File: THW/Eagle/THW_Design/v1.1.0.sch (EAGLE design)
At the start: 34 parts, among them U1 ADA4091-2ARZ-RL

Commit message: new version
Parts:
- removed JP1: (no value), pinhead:PINHD-2X10
- removed PAD1, PAD2, PAD4: (no value), wirepad:SMD5
- removed WP1: WIREPOINT_1A, WIREPOINT:WIREPOINT_1A
- added JP3: (no value), pinhead:PINHD-2X12
- added LONG_HW-: WIREPOINT_1A, WIREPOINT:WIREPOINT_1A
- added PAD5, PAD6, PAD7: (no value), wirepad:SMD5
- added PT$5, PT$6: PTS1206A, PTS1206:PTS1206A
- added TP1, TP13, TP14, TP15, TP16, TP17, TP18, TP19, TP2, TP20, TP21, TP22, TP23, TP24, TP25, TP26, TP27, TP28, TP3, TP4: TPTP10SQ, testpad:TPTP10SQ
- TP10, TP11, TP12, TP5, TP6, TP7, TP8, TP9: value TPSQTP09SQ -> TPTP10SQ; device testpad:TPSQTP09SQ -> testpad:TPTP10SQ
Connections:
- removed net T_S1+: JP1.1, PT$1.P$1, TP5.TP
- removed net T_S1-: JP1.2, PT$1.P$2, TP6.TP
- removed net T_S2+: JP1.3, PT$2.P$1, TP7.TP
- removed net T_S2-: JP1.4, PT$2.P$2, TP8.TP
- removed net T_S3+: JP1.5, PT$3.P$1, TP9.TP
- removed net T_S3-: JP1.6, PT$3.P$2, TP10.TP
- removed net T_S4+: JP1.7, PT$4.P$1, TP11.TP
- removed net T_S4-: JP1.8, PT$4.P$2, TP12.TP
- new net LONG_HW_SENS+: LONG_HW+.P$2, TP27.TP
- new net LONG_HW_SENS-: LONG_HW-.P$1, TP28.TP
- new net PT1_+: JP3.1, PT$2.+, TP1.TP
- new net PT1_-: JP3.2, PT$2.-, TP3.TP
- new net PT1_S+: JP3.3, PT$2.S+, TP2.TP
- new net PT1_S-: JP3.4, PT$2.S-, TP4.TP
- new net PT2_+: JP3.5, PT$3.+, TP5.TP
- new net PT2_-: JP3.6, PT$3.-, TP7.TP
- new net PT2_S+: JP3.7, PT$3.S+, TP6.TP
- new net PT2_S-: JP3.8, PT$3.S-, TP8.TP
- new net PT3_+: JP3.9, PT$1.+, TP9.TP
- new net PT3_-: JP3.10, PT$1.-, TP11.TP
- new net PT3_S+: JP3.11, PT$1.S+, TP10.TP
- new net PT3_S-: JP3.12, PT$1.S-, TP12.TP
- new net PT4_+: JP3.13, PT$4.+, TP13.TP
- new net PT4_-: JP3.14, PT$4.-, TP15.TP
- new net PT4_S+: JP3.15, PT$4.S+, TP14.TP
- new net PT4_S-: JP3.16, PT$4.S-, TP16.TP
- new net PT5_+: JP3.17, PT$5.+, TP17.TP
- new net PT5_-: JP3.18, PT$5.-, TP19.TP
- new net PT5_S+: JP3.19, PT$5.S+, TP18.TP
- new net PT5_S-: JP3.20, PT$5.S-, TP20.TP
- new net PT6_+: JP3.21, PT$6.+, TP21.TP
- new net PT6_-: JP3.22, PT$6.-, TP23.TP
- new net PT6_S+: JP3.23, PT$6.S+, TP22.TP
- new net PT6_S-: JP3.24, PT$6.S-, TP24.TP
- new net SHORT_HW_SENS+: SHORT_HW+.P$2, TP26.TP
- new net SHORT_HW_SENS-: SHORT_HW-.P$1, TP25.TP
- net LONG_HW+: now also PAD7.P; no longer PAD4.P, SV1.1
- net LONG_HW-: now also LONG_HW-.P$2; no longer SV1.2, WP1.P$1
- net SHORT_HW+: now also PAD5.P; no longer PAD1.P, SV1.35
- net SHORT_HW-: now also PAD6.P, SHORT_HW-.P$2; no longer PAD2.P, SHORT_HW-.P$1, SV1.36
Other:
- note removed: "Nanofluids: THW"
- moved on the sheet: C1, PAD3, R1, R2, R3, U1

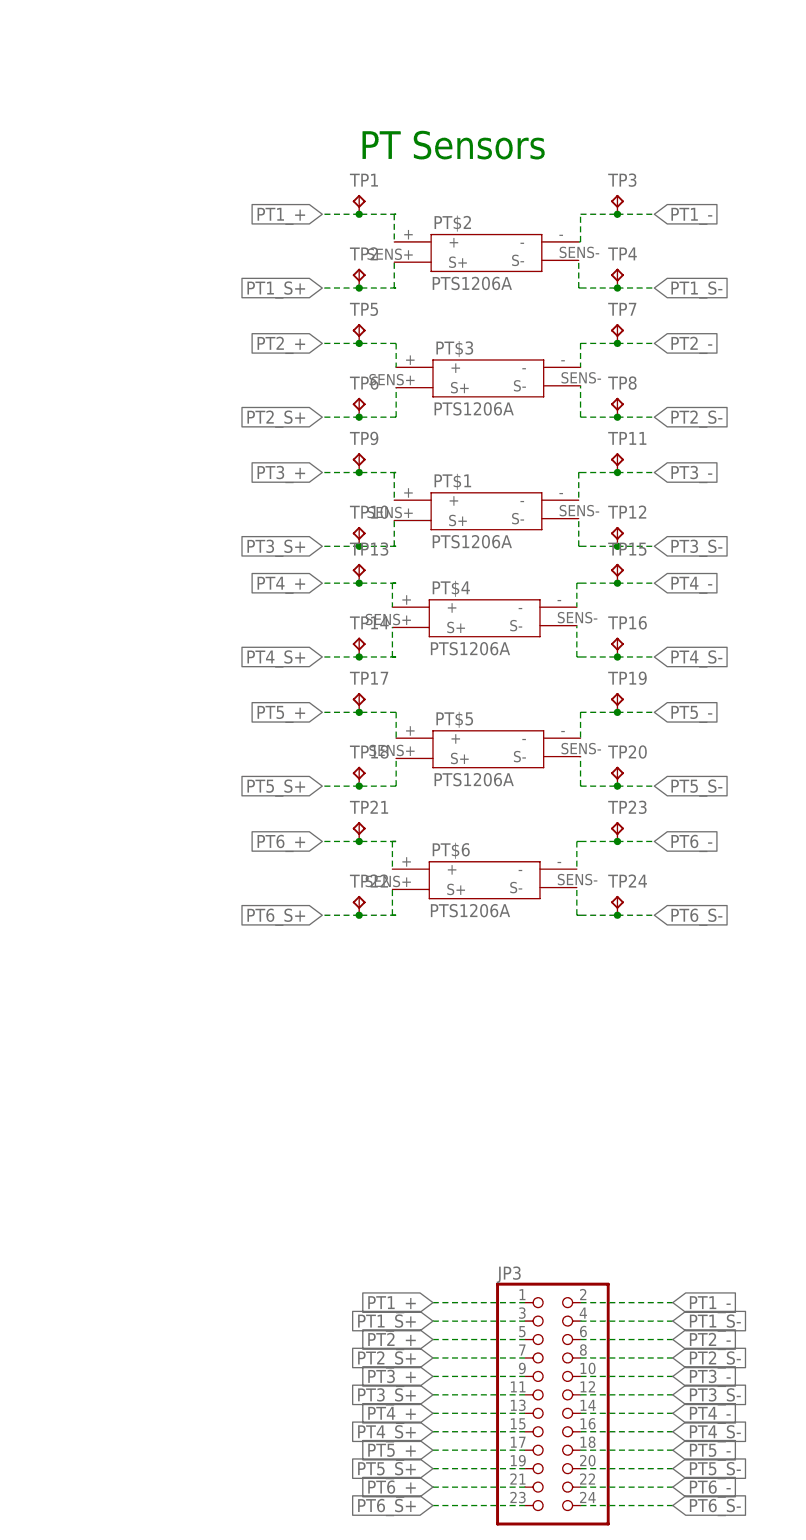
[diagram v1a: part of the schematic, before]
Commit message: adding one current source to PT sensors
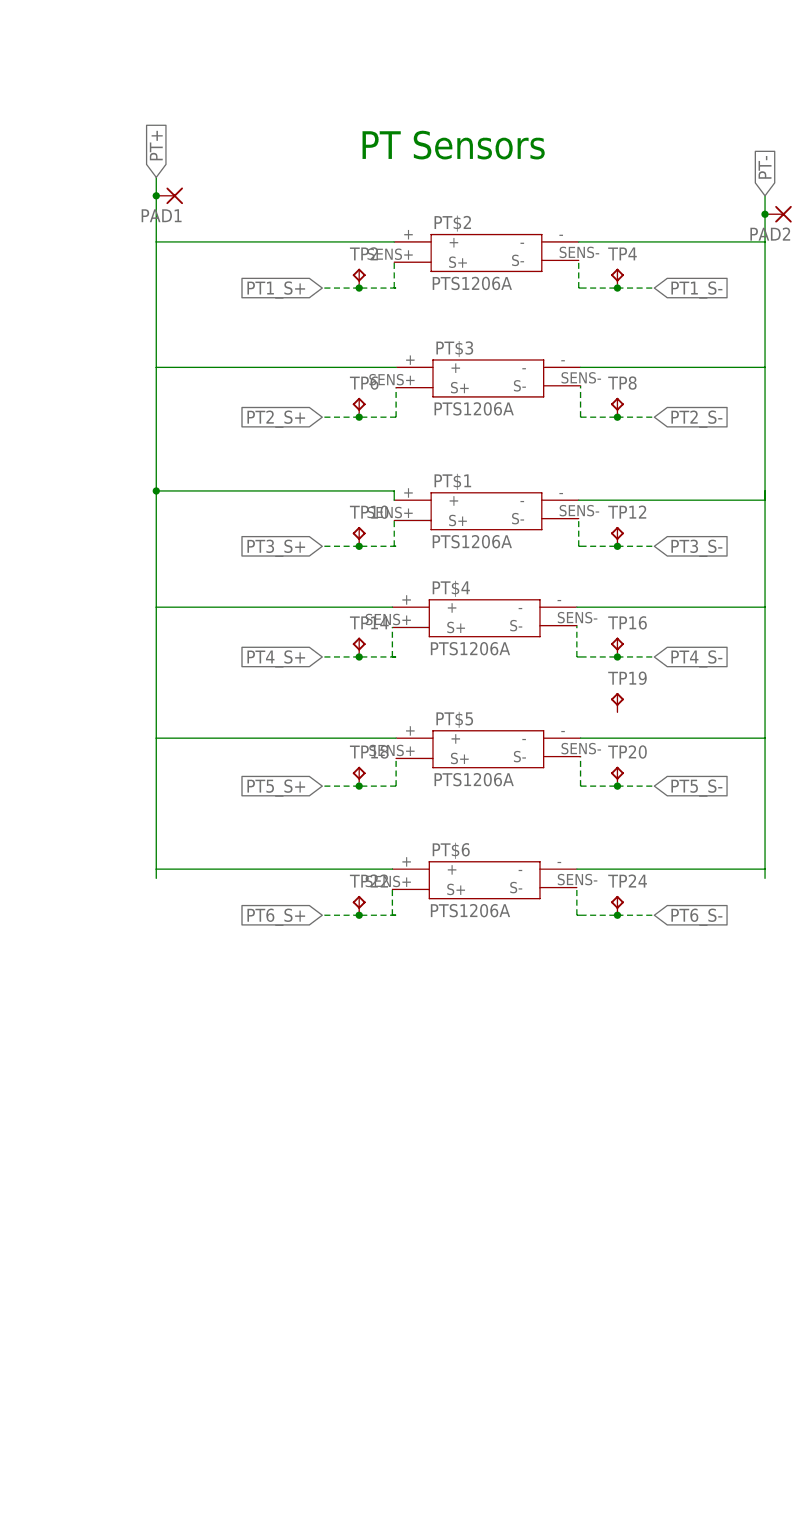
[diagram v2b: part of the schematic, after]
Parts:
- removed JP3: (no value), pinhead:PINHD-2X12
- removed TP1, TP11, TP13, TP15, TP17, TP21, TP23, TP3, TP5, TP7, TP9: TPTP10SQ, testpad:TPTP10SQ
- added PAD1, PAD2: (no value), wirepad:SMD5
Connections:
- removed net PT1_+: JP3.1, PT$2.+, TP1.TP
- removed net PT1_-: JP3.2, PT$2.-, TP3.TP
- removed net PT2_+: JP3.5, PT$3.+, TP5.TP
- removed net PT2_-: JP3.6, PT$3.-, TP7.TP
- removed net PT3_+: JP3.9, PT$1.+, TP9.TP
- removed net PT3_-: JP3.10, PT$1.-, TP11.TP
- removed net PT4_+: JP3.13, PT$4.+, TP13.TP
- removed net PT4_-: JP3.14, PT$4.-, TP15.TP
- removed net PT5_+: JP3.17, PT$5.+, TP17.TP
- removed net PT5_-: JP3.18, PT$5.-, TP19.TP
- removed net PT6_+: JP3.21, PT$6.+, TP21.TP
- removed net PT6_-: JP3.22, PT$6.-, TP23.TP
- new net B$2: PT$1.-
- new net PT+: PAD1.P, PT$1.+, PT$2.+, PT$3.+, PT$4.+, PT$5.+, PT$6.+
- new net PT-: PAD2.P, PT$2.-, PT$3.-, PT$4.-, PT$5.-, PT$6.-
- net PT1_S+: no longer JP3.3
- net PT1_S-: no longer JP3.4
- net PT2_S+: no longer JP3.7
- net PT2_S-: no longer JP3.8
- net PT3_S+: no longer JP3.11
- net PT3_S-: no longer JP3.12
- net PT4_S+: no longer JP3.15
- net PT4_S-: no longer JP3.16
- net PT5_S+: no longer JP3.19
- net PT5_S-: no longer JP3.20
- net PT6_S+: no longer JP3.23
- net PT6_S-: no longer JP3.24

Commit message: routing
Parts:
- removed C2: 0805YC103J4T2A, 0805YC103J4T2A:0805YC103J4T2A
- removed JP2: (no value), pinhead:PINHD-1X2
- removed LONGWIRE_VAR, SHORTWIRE_VAR: (no value), resistor:R-US_M0805
- removed PAD1, PAD2, PAD3, PAD5, PAD6, PAD7: (no value), wirepad:SMD5
- removed PT$6: PTS1206A, PTS1206:PTS1206A
- removed SV1: (no value), con-lstb:MA18-2
- removed TP19: TPTP10SQ, testpad:TPTP10SQ
- added POWER, PT_SENS1, PT_SENS2, WB_SENS1, WB_SENS2: RJ45_CONNECTOR, RJ45_CONNECTOR:RJ45_CONNECTOR
- added PT$0: PTS1206A, PTS1206:PTS1206A
- added TP1, TP3: TPTP10SQ, testpad:TPTP10SQ
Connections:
- removed net B$2: PT$1.-
- removed net LONG_HW_SENS+: LONG_HW+.P$2, TP27.TP
- removed net PT+: PAD1.P, PT$1.+, PT$2.+, PT$3.+, PT$4.+, PT$5.+, PT$6.+
- removed net PT-: PAD2.P, PT$2.-, PT$3.-, PT$4.-, PT$5.-, PT$6.-
- removed net PT6_S+: PT$6.S+, TP22.TP
- removed net PT6_S-: PT$6.S-, TP24.TP
- new net PT0_S+: PT$0.S+, PT_SENS2.3, TP2.TP
- new net PT0_S-: PT$0.S-, PT_SENS2.4, TP4.TP
- new net PT_CURRENT+: POWER.7, PT$0.+, PT$0.-, PT$1.+, PT$1.-, PT$2.+, PT$2.-, PT$3.+, PT$3.-, PT$4.+, PT$4.-, PT$5.+, TP1.TP
- new net PT_CURRENT-: POWER.8, PT$5.-, TP3.TP
- new net WB_CURRENT+: POWER.3, R_CURRENT.1, WB_SENS2.1
- new net WB_CURRENT-: LONG_HW-.P$2, POWER.4, R7.1, WB_SENS2.6
- net GND: now also POWER.6, WB_SENS2.8; no longer C2.C2, JP2.1, LONGWIRE_VAR.2, R7.1, SV1.25, SV1.4
- net LONG_HW+: no longer LONG_HW+.P$1, PAD7.P, SHORTWIRE_VAR.1, SV1.24, SV1.27
- net LONG_HW-: no longer LONGWIRE_VAR.1, LONG_HW-.P$2, PAD3.P, SV1.26
- net LONG_HW_SENS-: now also WB_SENS1.2
- net OPAMP_OUTPUT: now also WB_SENS2.7; no longer SV1.3
- net PT1_S+: now also PT$1.S+, PT_SENS1.2, TP10.TP; no longer PT$2.S+, TP2.TP
- net PT1_S-: now also PT$1.S-, PT_SENS1.1, TP12.TP; no longer PT$2.S-, TP4.TP
- net PT2_S+: now also PT$2.S+, PT_SENS2.5; no longer PT$3.S+
- net PT2_S-: now also PT$2.S-, PT_SENS2.6; no longer PT$3.S-
- net PT3_S+: now also PT$3.S+, PT_SENS2.2, TP18.TP; no longer PT$1.S+, TP10.TP
- net PT3_S-: now also PT$3.S-, PT_SENS2.1, TP20.TP; no longer PT$1.S-, TP12.TP
- net PT4_S+: now also PT_SENS2.8
- net PT4_S-: now also PT_SENS2.7
- net PT5_S+: now also PT_SENS1.4, TP22.TP; no longer TP18.TP
- net PT5_S-: now also PT_SENS1.3, TP24.TP; no longer TP20.TP
- net SHORT_HW+: now also WB_SENS2.2, WB_SENS2.3; no longer PAD5.P, SV1.30
- net SHORT_HW-: now also LONG_HW+.P$1; no longer PAD6.P, SHORTWIRE_VAR.2, SV1.28
- net SHORT_HW_SENS+: now also WB_SENS1.8
- net SHORT_HW_SENS-: now also LONG_HW+.P$2, TP27.TP, WB_SENS1.1, WB_SENS1.5, WB_SENS1.7
- net SUMMING_OP_AMP: now also WB_SENS1.6, WB_SENS2.4, WB_SENS2.5; no longer SV1.23
- net VSS: now also POWER.5; no longer C2.C1, JP2.2, R_CURRENT.1, SV1.29
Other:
- note removed: "NODE B"
- note removed: "POWER PIN"
- note removed: "SENSE PINS"
- note removed: "WIRES"
